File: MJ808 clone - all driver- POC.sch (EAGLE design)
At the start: 42 parts, among them IC1 ATTINY4313-MMH, IC2 PRQV8.00CR1510Y00L, IC3 LP38693SD-5.0/NOPB, IC4 MCP2515, IC5 LP38693SD-5.0/NOPB, IC6 MCP2561-2, IC7 MAX16820, K1 CRTL, Q1 PMV213SN,215, X1 22-23-2021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

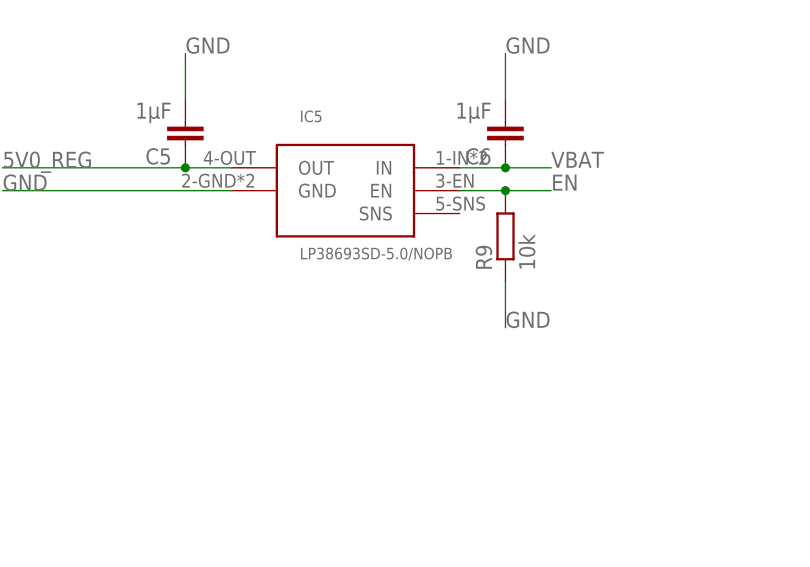
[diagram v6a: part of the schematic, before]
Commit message: - minor corrections in BOM and LDO schematic
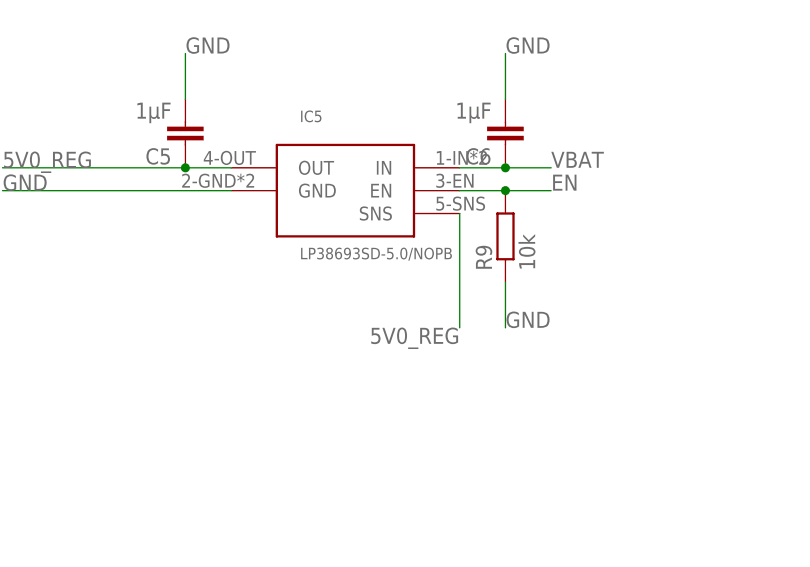
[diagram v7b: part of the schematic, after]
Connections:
- net 5V0_REG: now also IC5.SNS
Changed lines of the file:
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@@
 <grid distance="0.1" unitdist="inch" unit="inch" style="lines" multiple="1" display="no" altdistance="0.01" altunitdist="inch" altunit="inch"/>
 <layers>
-<layer number="1" name="Top" color="4" fill="1" visible="yes" active="no"/>
-<layer number="2" name="Route2" color="1" fill="3" visible="yes" active="no"/>
-<layer number="3" name="Route3" color="4" fill="3" visible="yes" active="no"/>
-<layer number="4" name="Route4" color="1" fill="4" visible="yes" active="no"/>
-<layer number="5" name="Route5" color="4" fill="4" visible="yes" active="no"/>
-<layer number="6" name="Route6" color="1" fill="8" visible="yes" active="no"/>
-<layer number="7" name="Route7" color="4" fill="8" visible="yes" active="no"/>
-<layer number="8" name="Route8" color="1" fill="2" visible="yes" active="no"/>
-<layer number="9" name="Route9" color="4" fill="2" visible="yes" active="no"/>
-<layer number="10" name="Route10" color="1" fill="7" visible="yes" active="no"/>
-<layer number="11" name="Route11" color="4" fill="7" visible="yes" active="no"/>
-<layer number="12" name="Route12" color="1" fill="5" visible="yes" active="no"/>
-<layer number="13" name="Route13" color="4" fill="5" visible="yes" active="no"/>
-<layer number="14" name="Route14" color="1" fill="6" visible="yes" active="no"/>
-<layer number="15" name="Route15" color="4" fill="6" visible="yes" active="no"/>
-<layer number="16" name="Bottom" color="1" fill="1" visible="yes" active="no"/>
-<layer number="17" name="Pads" color="2" fill="1" visible="yes" active="no"/>
-<layer number="18" name="Vias" color="2" fill="1" visible="yes" active="no"/>
-<layer number="19" name="Unrouted" color="6" fill="1" visible="yes" active="no"/>
-<layer number="20" name="Dimension" color="24" fill="1" visible="yes" active="no"/>
-<layer number="21" name="tPlace" color="7" fill="1" visible="yes" active="no"/>
-<layer number="22" name="bPlace" color="7" fill="1" visible="yes" active="no"/>
-<layer number="23" name="tOrigins" color="15" fill="1" visible="yes" active="no"/>
-<layer number="24" name="bOrigins" color="15" fill="1" visible="yes" active="no"/>
-<layer number="25" name="tNames" color="7" fill="1" visible="yes" active="no"/>
-<layer number="26" name="bNames" color="7" fill="1" visible="yes" active="no"/>
-<layer number="27" name="tValues" color="7" fill="1" visible="yes" active="no"/>
-<layer number="28" name="bValues" color="7" fill="1" visible="yes" active="no"/>
+<layer number="1" name="Top" color="4" fill="1" visible="no" active="no"/>
+<layer number="2" name="Route2" color="1" fill="3" visible="no" active="no"/>
+<layer number="3" name="Route3" color="4" fill="3" visible="no" active="no"/>
+<layer number="4" name="Route4" color="1" fill="4" visible="no" active="no"/>
+<layer number="5" name="Route5" color="4" fill="4" visible="no" active="no"/>
+<layer number="6" name="Route6" color="1" fill="8" visible="no" active="no"/>
+<layer number="7" name="Route7" color="4" fill="8" visible="no" active="no"/>
+<layer number="8" name="Route8" color="1" fill="2" visible="no" active="no"/>
+<layer number="9" name="Route9" color="4" fill="2" visible="no" active="no"/>
+<layer number="10" name="Route10" color="1" fill="7" visible="no" active="no"/>
+<layer number="11" name="Route11" color="4" fill="7" visible="no" active="no"/>
+<layer number="12" name="Route12" color="1" fill="5" visible="no" active="no"/>
+<layer number="13" name="Route13" color="4" fill="5" visible="no" active="no"/>
+<layer number="14" name="Route14" color="1" fill="6" visible="no" active="no"/>
+<layer number="15" name="Route15" color="4" fill="6" visible="no" active="no"/>
+<layer number="16" name="Bottom" color="1" fill="1" visible="no" active="no"/>
+<layer number="17" name="Pads" color="2" fill="1" visible="no" active="no"/>
+<layer number="18" name="Vias" color="2" fill="1" visible="no" active="no"/>
+<layer number="19" name="Unrouted" color="6" fill="1" visible="no" active="no"/>
+<layer number="20" name="Dimension" color="24" fill="1" visible="no" active="no"/>
+<layer number="21" name="tPlace" color="7" fill="1" visible="no" active="no"/>
+<layer number="22" name="bPlace" color="7" fill="1" visible="no" active="no"/>
+<layer number="23" name="tOrigins" color="15" fill="1" visible="no" active="no"/>
+<layer number="24" name="bOrigins" color="15" fill="1" visible="no" active="no"/>
+<layer number="25" name="tNames" color="7" fill="1" visible="no" active="no"/>
+<layer number="26" name="bNames" color="7" fill="1" visible="no" active="no"/>
+<layer number="27" name="tValues" color="7" fill="1" visible="no" active="no"/>
+<layer number="28" name="bValues" color="7" fill="1" visible="no" active="no"/>
 <layer number="29" name="tStop" color="7" fill="3" visible="no" active="no"/>
 <layer number="30" name="bStop" color="7" fill="6" visible="no" active="no"/>
@@
 <layer number="35" name="tGlue" color="7" fill="4" visible="no" active="no"/>
 <layer number="36" name="bGlue" color="7" fill="5" visible="no" active="no"/>
-<layer number="37" name="tTest" color="7" fill="1" visible="yes" active="no"/>
-<layer number="38" name="bTest" color="7" fill="1" visible="yes" active="no"/>
+<layer number="37" name="tTest" color="7" fill="1" visible="no" active="no"/>
+<layer number="38" name="bTest" color="7" fill="1" visible="no" active="no"/>
 <layer number="39" name="tKeepout" color="4" fill="11" visible="no" active="no"/>
 <layer number="40" name="bKeepout" color="1" fill="11" visible="no" active="no"/>
@@
 <layer number="44" name="Drills" color="7" fill="1" visible="no" active="no"/>
 <layer number="45" name="Holes" color="7" fill="1" visible="no" active="no"/>
-<layer number="46" name="Milling" color="3" fill="1" visible="yes" active="no"/>
-<layer number="47" name="Measures" color="7" fill="1" visible="yes" active="no"/>
-<layer number="48" name="Document" color="7" fill="1" visible="yes" active="no"/>
-<layer number="49" name="Reference" color="7" fill="1" visible="yes" active="no"/>
-<layer number="50" name="dxf" color="7" fill="1" visible="yes" active="no"/>
-<layer number="51" name="tDocu" color="7" fill="1" visible="yes" active="no"/>
-<layer number="52" name="bDocu" color="7" fill="1" visible="yes" active="no"/>
-<layer number="53" name="tGND_GNDA" color="7" fill="9" visible="yes" active="no"/>
-<layer number="54" name="bGND_GNDA" color="1" fill="9" visible="yes" active="no"/>
-<layer number="56" name="wert" color="7" fill="1" visible="yes" active="no"/>
-<layer number="57" name="tCAD" color="7" fill="1" visible="yes" active="no"/>
-<layer number="59" name="tCarbon" color="7" fill="1" visible="yes" active="no"/>
-<layer number="60" name="bCarbon" color="7" fill="1" visible="yes" active="no"/>
+<layer number="46" name="Milling" color="3" fill="1" visible="no" active="no"/>
+<layer number="47" name="Measures" color="7" fill="1" visible="no" active="no"/>
+<layer number="48" name="Document" color="7" fill="1" visible="no" active="no"/>
+<layer number="49" name="Reference" color="7" fill="1" visible="no" active="no"/>
+<layer number="50" name="dxf" color="7" fill="1" visible="no" active="no"/>
+<layer number="51" name="tDocu" color="7" fill="1" visible="no" active="no"/>
+<layer number="52" name="bDocu" color="7" fill="1" visible="no" active="no"/>
+<layer number="53" name="tGND_GNDA" color="7" fill="9" visible="no" active="no"/>
+<layer number="54" name="bGND_GNDA" color="1" fill="9" visible="no" active="no"/>
+<layer number="56" name="wert" color="7" fill="1" visible="no" active="no"/>
+<layer number="57" name="tCAD" color="7" fill="1" visible="no" active="no"/>
+<layer number="59" name="tCarbon" color="7" fill="1" visible="no" active="no"/>
+<layer number="60" name="bCarbon" color="7" fill="1" visible="no" active="no"/>
 <layer number="88" name="SimResults" color="9" fill="1" visible="yes" active="yes"/>
 <layer number="89" name="SimProbes" color="9" fill="1" visible="yes" active="yes"/>
@@
 <label x="368.3" y="38.1" size="1.778" layer="95"/>
 </segment>
-</net>
+<segment>
+<pinref part="IC5" gate="G$1" pin="SNS"/>
+<wire x1="266.7" y1="175.26" x2="266.7" y2="162.56" width="0.1524" layer="91"/>
+<label x="266.7" y="162.56" size="1.778" layer="95" rot="R180"/>
+</segment>
+</net>

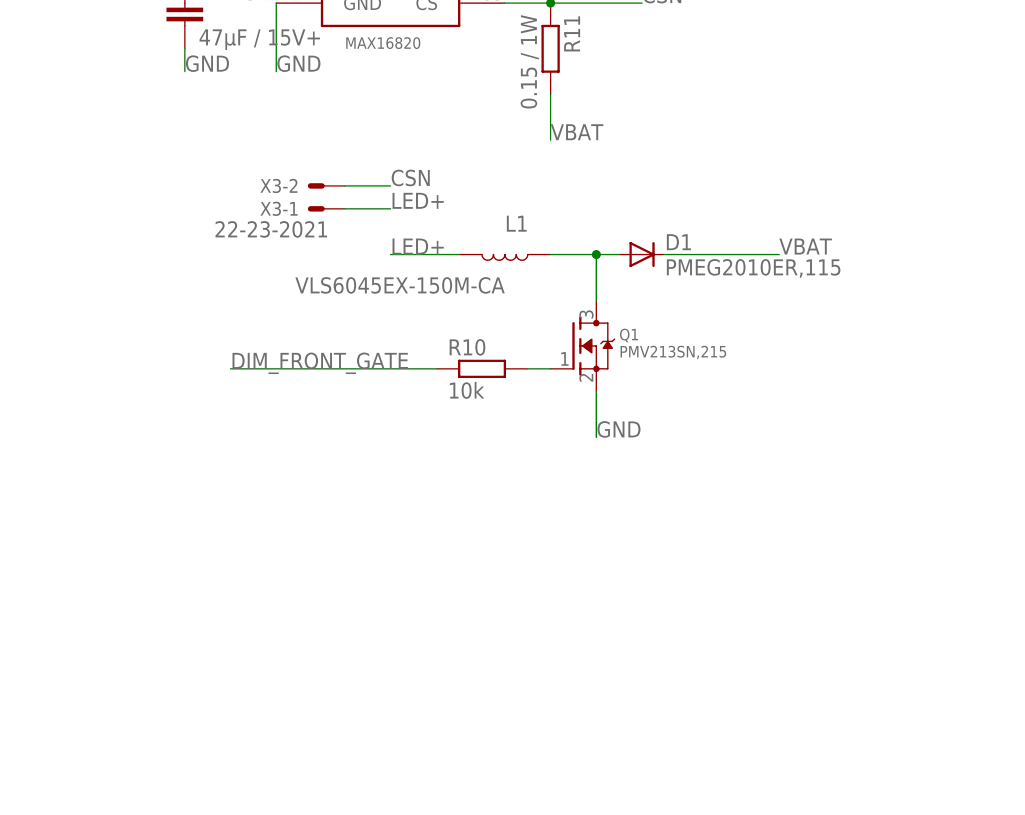
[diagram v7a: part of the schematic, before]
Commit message: - added LED description to LED connector
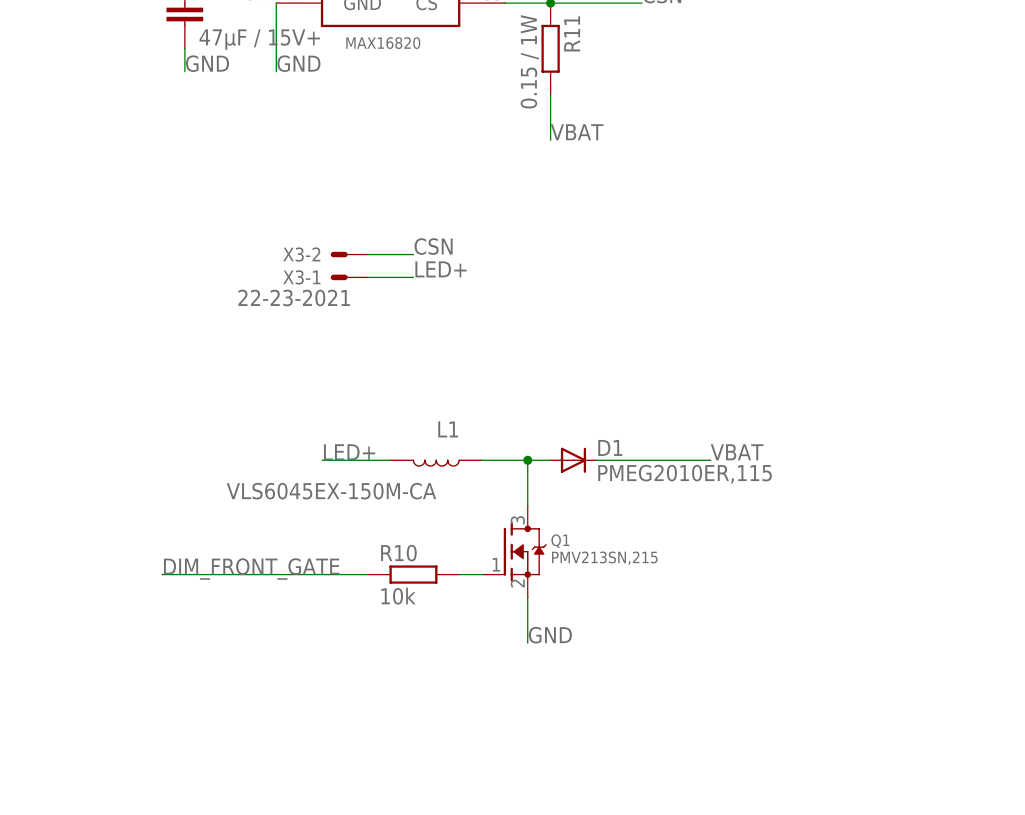
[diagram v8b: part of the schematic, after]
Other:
- note added: "white LED Cree XMLBWT-00-0000-0000U20E2"
- moved on the sheet: D1, L1, Q1, R10, X3-1, X3-2
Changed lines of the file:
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@@
 <text x="236.22" y="208.28" size="1.778" layer="90">power supply for microcontroller</text>
 <text x="330.2" y="213.36" size="1.778" layer="90">white LED driver</text>
+<text x="360.68" y="157.48" size="1.778" layer="90">white LED
+Cree XMLBWT-00-0000-0000U20E2</text>
 </plain>
 <instances>
 <instance part="R11" gate="G$1" x="368.3" y="182.88" rot="R270"/>
 <instance part="C8" gate="G$1" x="327.66" y="187.96"/>
-<instance part="D1" gate="G$1" x="378.46" y="160.02"/>
-<instance part="L1" gate="G$1" x="363.22" y="160.02" smashed="yes" rot="R270">
-<attribute name="NAME" x="363.22" y="162.56" size="1.778" layer="95"/>
-<attribute name="VALUE" x="363.22" y="157.48" size="1.778" layer="96" rot="R180"/>
+<instance part="D1" gate="G$1" x="370.84" y="137.16"/>
+<instance part="L1" gate="G$1" x="355.6" y="137.16" smashed="yes" rot="R270">
+<attribute name="NAME" x="355.6" y="139.7" size="1.778" layer="95"/>
+<attribute name="VALUE" x="355.6" y="134.62" size="1.778" layer="96" rot="R180"/>
 </instance>
-<instance part="Q1" gate="G$1" x="370.84" y="149.86"/>
+<instance part="Q1" gate="G$1" x="363.22" y="127"/>
 <instance part="IC4" gate="G$1" x="248.92" y="50.8"/>
 <instance part="IC6" gate="G$1" x="342.9" y="58.42"/>
@@
 <instance part="C4" gate="G$1" x="210.82" y="35.56"/>
 <instance part="C1" gate="G$1" x="93.98" y="187.96" rot="R180"/>
-<instance part="R10" gate="G$1" x="360.68" y="147.32"/>
+<instance part="R10" gate="G$1" x="353.06" y="124.46"/>
 <instance part="R7" gate="G$1" x="205.74" y="50.8" rot="R90"/>
 <instance part="R4" gate="G$1" x="170.18" y="170.18" rot="R90"/>
@@
 <instance part="K1" gate="G$1" x="25.4" y="33.02"/>
 <instance part="R9" gate="G$1" x="271.78" y="172.72" rot="R90"/>
-<instance part="X3" gate="-1" x="342.9" y="165.1" rot="R180"/>
-<instance part="X3" gate="-2" x="342.9" y="167.64" rot="R180"/>
+<instance part="X3" gate="-1" x="345.44" y="157.48" rot="R180"/>
+<instance part="X3" gate="-2" x="345.44" y="160.02" rot="R180"/>
 <instance part="C2" gate="G$1" x="106.68" y="50.8" rot="R180"/>
 <instance part="IC3" gate="G$1" x="124.46" y="45.72"/>
@@
 <segment>
 <pinref part="D1" gate="G$1" pin="C"/>
-<wire x1="381" y1="160.02" x2="393.7" y2="160.02" width="0.1524" layer="91"/>
-<label x="393.7" y="160.02" size="1.778" layer="95"/>
+<wire x1="373.38" y1="137.16" x2="386.08" y2="137.16" width="0.1524" layer="91"/>
+<label x="386.08" y="137.16" size="1.778" layer="95"/>
 </segment>
 <segment>
@@
 <segment>
 <pinref part="Q1" gate="G$1" pin="S"/>
-<wire x1="373.38" y1="144.78" x2="373.38" y2="139.7" width="0.1524" layer="91"/>
-<label x="373.38" y="139.7" size="1.778" layer="95"/>
+<wire x1="365.76" y1="121.92" x2="365.76" y2="116.84" width="0.1524" layer="91"/>
+<label x="365.76" y="116.84" size="1.778" layer="95"/>
 </segment>
 <segment>
@@
 <segment>
 <pinref part="X3" gate="-2" pin="S"/>
-<wire x1="345.44" y1="167.64" x2="350.52" y2="167.64" width="0.1524" layer="91"/>
-<label x="350.52" y="167.64" size="1.778" layer="95"/>
+<wire x1="347.98" y1="160.02" x2="353.06" y2="160.02" width="0.1524" layer="91"/>
+<label x="353.06" y="160.02" size="1.778" layer="95"/>
 </segment>
 </net>
@@
 <pinref part="Q1" gate="G$1" pin="G"/>
 <pinref part="R10" gate="G$1" pin="2"/>
-<wire x1="365.76" y1="147.32" x2="368.3" y2="147.32" width="0.1524" layer="91"/>
+<wire x1="358.14" y1="124.46" x2="360.68" y2="124.46" width="0.1524" layer="91"/>
 </segment>
 </net>
@@
 <segment>
 <pinref part="Q1" gate="G$1" pin="D"/>
-<wire x1="373.38" y1="154.94" x2="373.38" y2="160.02" width="0.1524" layer="91"/>
+<wire x1="365.76" y1="132.08" x2="365.76" y2="137.16" width="0.1524" layer="91"/>
 <pinref part="D1" gate="G$1" pin="A"/>
-<wire x1="373.38" y1="160.02" x2="375.92" y2="160.02" width="0.1524" layer="91"/>
+<wire x1="365.76" y1="137.16" x2="368.3" y2="137.16" width="0.1524" layer="91"/>
 <pinref part="L1" gate="G$1" pin="1"/>
-<wire x1="368.3" y1="160.02" x2="373.38" y2="160.02" width="0.1524" layer="91"/>
-<junction x="373.38" y="160.02"/>
+<wire x1="360.68" y1="137.16" x2="365.76" y2="137.16" width="0.1524" layer="91"/>
+<junction x="365.76" y="137.16"/>
 </segment>
 </net>
@@
 <segment>
 <pinref part="R10" gate="G$1" pin="1"/>
-<wire x1="355.6" y1="147.32" x2="332.74" y2="147.32" width="0.1524" layer="91"/>
-<label x="332.74" y="147.32" size="1.778" layer="95"/>
+<wire x1="347.98" y1="124.46" x2="325.12" y2="124.46" width="0.1524" layer="91"/>
+<label x="325.12" y="124.46" size="1.778" layer="95"/>
 </segment>
 <segment>
@@
 <segment>
 <pinref part="L1" gate="G$1" pin="2"/>
-<wire x1="350.52" y1="160.02" x2="358.14" y2="160.02" width="0.1524" layer="91"/>
-<label x="350.52" y="160.02" size="1.778" layer="95"/>
+<wire x1="342.9" y1="137.16" x2="350.52" y2="137.16" width="0.1524" layer="91"/>
+<label x="342.9" y="137.16" size="1.778" layer="95"/>
 </segment>
 <segment>
 <pinref part="X3" gate="-1" pin="S"/>
-<wire x1="345.44" y1="165.1" x2="350.52" y2="165.1" width="0.1524" layer="91"/>
-<label x="350.52" y="165.1" size="1.778" layer="95"/>
+<wire x1="347.98" y1="157.48" x2="353.06" y2="157.48" width="0.1524" layer="91"/>
+<label x="353.06" y="157.48" size="1.778" layer="95"/>
 </segment>
 </net>
@@
 </drawing>
 <compatibility>
+<note version="6.3" minversion="6.2.2" severity="warning">
+Since Version 6.2.2 text objects can contain more than one line,
+which will not be processed correctly with this version.
+</note>
 <note version="8.2" severity="warning">
 Since Version 8.2, EAGLE supports online libraries. The ids
